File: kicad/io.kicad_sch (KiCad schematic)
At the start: 12 parts, among them J10 IO6, J5 IO1, J6 IO2, J7 IO3, J8 IO4, J9 IO5

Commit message: Lay out rev 2 with an internal pack, protector and cost-down parts
Board is 91 x 47 mm for a 96 x 52 mm enclosure, with placement and hand
power routing done; signal routing is still to do.

- Internal Gens Ace 3S 1000 mAh pack on an XT60 pigtail, protected on the
  board by a BQ7791501 with back-to-back low-side FETs and a 2.5 mOhm
  shunt, plus a balance header and two NTCs.
- USB-A and USB-C on the top edge, IO as a recessed 3 x 6 pin block, GPIO
  map re-swapped for the placement, USB nets renamed with P/N suffixes
  for the diff-pair router.
- Cost-down swaps that keep every feature: basic or preferred passives
  and ICs, cheaper connectors, a THT power switch rated for 12.6 V, and
  replacements for the low-stock TH1 and Q2/Q3. L3 is Digi-Key sourced
  and hand-placed.
- Net classes and design rules, rev 2 power-net widths in review.py, and
  the PCB critic and loop updated for rev 2.

Schematic review passes; PCB review passes every gate except unrouted.

Co-Authored-By: Claude Opus 5.5 <noreply@anthropic.com>
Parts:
- J10, J5, J6, J7, J8, J9: footprint Connector_PinHeader_2.54mm:PinHeader_1x03_P2.54mm_Horizontal -> Connector_PinHeader_2.54mm:PinHeader_1x03_P2.54mm_Vertical; LCSC Part # C32713262 -> C49257; MPN HX PZ2.54-1x3P WZ -> 2.54-1*3P; Manufacturer hanxia -> BOOMELE(Boom Precision Elec)
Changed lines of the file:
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@@
 			)
 		)
-		(property "Footprint" "Connector_PinHeader_2.54mm:PinHeader_1x03_P2.54mm_Horizontal"
+		(property "Footprint" "Connector_PinHeader_2.54mm:PinHeader_1x03_P2.54mm_Vertical"
 			(at 129.54 48.26 0)
 			(hide yes)
@@
 			)
 		)
-    (property "MPN" "HX PZ2.54-1x3P WZ" (at 129.54 48.26 0)
-      (effects (font (size 1.27 1.27)) (hide yes))
-    )
-    (property "Manufacturer" "hanxia" (at 129.54 48.26 0)
-      (effects (font (size 1.27 1.27)) (hide yes))
-    )
-    (property "LCSC Part #" "C32713262" (at 129.54 48.26 0)
+    (property "MPN" "2.54-1*3P" (at 129.54 48.26 0)
+      (effects (font (size 1.27 1.27)) (hide yes))
+    )
+    (property "Manufacturer" "BOOMELE(Boom Precision Elec)" (at 129.54 48.26 0)
+      (effects (font (size 1.27 1.27)) (hide yes))
+    )
+    (property "LCSC Part #" "C49257" (at 129.54 48.26 0)
       (effects (font (size 1.27 1.27)) (hide yes))
     )
@@
 			)
 		)
-		(property "Footprint" "Connector_PinHeader_2.54mm:PinHeader_1x03_P2.54mm_Horizontal"
+		(property "Footprint" "Connector_PinHeader_2.54mm:PinHeader_1x03_P2.54mm_Vertical"
 			(at 129.54 66.04 0)
 			(hide yes)
@@
 			)
 		)
-    (property "MPN" "HX PZ2.54-1x3P WZ" (at 129.54 66.04 0)
-      (effects (font (size 1.27 1.27)) (hide yes))
-    )
-    (property "Manufacturer" "hanxia" (at 129.54 66.04 0)
-      (effects (font (size 1.27 1.27)) (hide yes))
-    )
-    (property "LCSC Part #" "C32713262" (at 129.54 66.04 0)
+    (property "MPN" "2.54-1*3P" (at 129.54 66.04 0)
+      (effects (font (size 1.27 1.27)) (hide yes))
+    )
+    (property "Manufacturer" "BOOMELE(Boom Precision Elec)" (at 129.54 66.04 0)
+      (effects (font (size 1.27 1.27)) (hide yes))
+    )
+    (property "LCSC Part #" "C49257" (at 129.54 66.04 0)
       (effects (font (size 1.27 1.27)) (hide yes))
     )
@@
 			)
 		)
-		(property "Footprint" "Connector_PinHeader_2.54mm:PinHeader_1x03_P2.54mm_Horizontal"
+		(property "Footprint" "Connector_PinHeader_2.54mm:PinHeader_1x03_P2.54mm_Vertical"
 			(at 129.54 83.82 0)
 			(hide yes)
@@
 			)
 		)
-    (property "MPN" "HX PZ2.54-1x3P WZ" (at 129.54 83.82 0)
-      (effects (font (size 1.27 1.27)) (hide yes))
-    )
-    (property "Manufacturer" "hanxia" (at 129.54 83.82 0)
-      (effects (font (size 1.27 1.27)) (hide yes))
-    )
-    (property "LCSC Part #" "C32713262" (at 129.54 83.82 0)
+    (property "MPN" "2.54-1*3P" (at 129.54 83.82 0)
+      (effects (font (size 1.27 1.27)) (hide yes))
+    )
+    (property "Manufacturer" "BOOMELE(Boom Precision Elec)" (at 129.54 83.82 0)
+      (effects (font (size 1.27 1.27)) (hide yes))
+    )
+    (property "LCSC Part #" "C49257" (at 129.54 83.82 0)
       (effects (font (size 1.27 1.27)) (hide yes))
     )
@@
 			)
 		)
-		(property "Footprint" "Connector_PinHeader_2.54mm:PinHeader_1x03_P2.54mm_Horizontal"
+		(property "Footprint" "Connector_PinHeader_2.54mm:PinHeader_1x03_P2.54mm_Vertical"
 			(at 129.54 101.6 0)
 			(hide yes)
@@
 			)
 		)
-    (property "MPN" "HX PZ2.54-1x3P WZ" (at 129.54 101.6 0)
-      (effects (font (size 1.27 1.27)) (hide yes))
-    )
-    (property "Manufacturer" "hanxia" (at 129.54 101.6 0)
-      (effects (font (size 1.27 1.27)) (hide yes))
-    )
-    (property "LCSC Part #" "C32713262" (at 129.54 101.6 0)
+    (property "MPN" "2.54-1*3P" (at 129.54 101.6 0)
+      (effects (font (size 1.27 1.27)) (hide yes))
+    )
+    (property "Manufacturer" "BOOMELE(Boom Precision Elec)" (at 129.54 101.6 0)
+      (effects (font (size 1.27 1.27)) (hide yes))
+    )
+    (property "LCSC Part #" "C49257" (at 129.54 101.6 0)
       (effects (font (size 1.27 1.27)) (hide yes))
     )
@@
 			)
 		)
-		(property "Footprint" "Connector_PinHeader_2.54mm:PinHeader_1x03_P2.54mm_Horizontal"
+		(property "Footprint" "Connector_PinHeader_2.54mm:PinHeader_1x03_P2.54mm_Vertical"
 			(at 129.54 119.38 0)
 			(hide yes)
@@
 			)
 		)
-    (property "MPN" "HX PZ2.54-1x3P WZ" (at 129.54 119.38 0)
-      (effects (font (size 1.27 1.27)) (hide yes))
-    )
-    (property "Manufacturer" "hanxia" (at 129.54 119.38 0)
-      (effects (font (size 1.27 1.27)) (hide yes))
-    )
-    (property "LCSC Part #" "C32713262" (at 129.54 119.38 0)
+    (property "MPN" "2.54-1*3P" (at 129.54 119.38 0)
+      (effects (font (size 1.27 1.27)) (hide yes))
+    )
+    (property "Manufacturer" "BOOMELE(Boom Precision Elec)" (at 129.54 119.38 0)
+      (effects (font (size 1.27 1.27)) (hide yes))
+    )
+    (property "LCSC Part #" "C49257" (at 129.54 119.38 0)
       (effects (font (size 1.27 1.27)) (hide yes))
     )
@@
 			)
 		)
-		(property "Footprint" "Connector_PinHeader_2.54mm:PinHeader_1x03_P2.54mm_Horizontal"
+		(property "Footprint" "Connector_PinHeader_2.54mm:PinHeader_1x03_P2.54mm_Vertical"
 			(at 129.54 137.16 0)
 			(hide yes)
@@
 			)
 		)
-    (property "MPN" "HX PZ2.54-1x3P WZ" (at 129.54 137.16 0)
-      (effects (font (size 1.27 1.27)) (hide yes))
-    )
-    (property "Manufacturer" "hanxia" (at 129.54 137.16 0)
-      (effects (font (size 1.27 1.27)) (hide yes))
-    )
-    (property "LCSC Part #" "C32713262" (at 129.54 137.16 0)
-      (effects (font (size 1.27 1.27)) (hide yes))
-    )
+    (property "MPN" "2.54-1*3P" (at 129.54 137.16 0)
+      (effects (font (size 1.27 1.27)) (hide yes))
+    )
+    (property "Manufacturer" "BOOMELE(Boom Precision Elec)" (at 129.54 137.16 0)
+      (effects (font (size 1.27 1.27)) (hide yes))
+    )
+    (property "LCSC Part #" "C49257" (at 129.54 137.16 0)
+      (effects (font (size 1.27 1.27)) (hide yes))
+    )

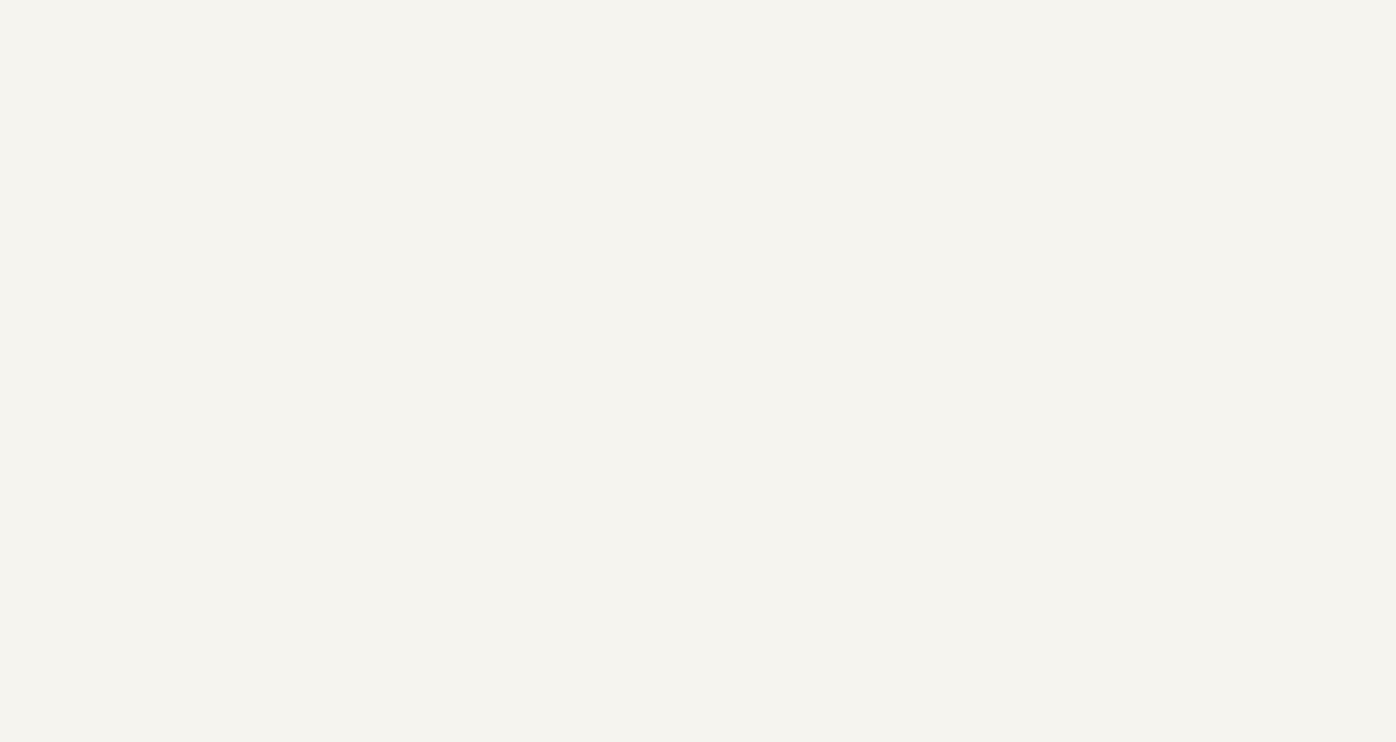
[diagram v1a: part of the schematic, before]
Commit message: Add a header for an external WS2812B LED stick
J12 (JST-PH 3-pin) feeds an 8-LED WS2812B stick mounted on the case's
top edge near the USB ports. GPIO21 drives it through a 74AHCT1G125 so
the data line reaches the 5 V VIH, with a 330 ohm series resistor and
10 uF at the connector. Power comes from the switched 5 V rail; firmware
should cap brightness (about 0.5 A at full white).

Co-Authored-By: Claude Opus 5.5 <noreply@anthropic.com>
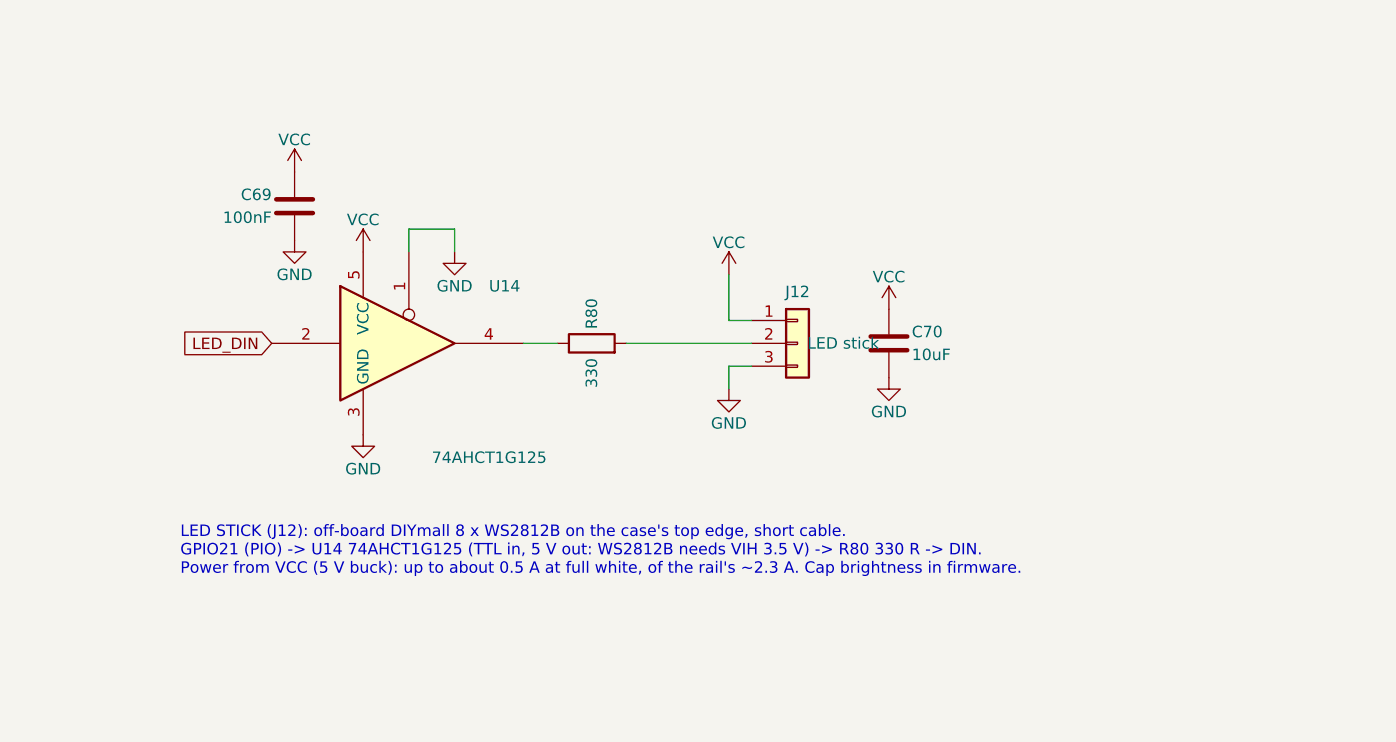
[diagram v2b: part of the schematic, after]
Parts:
- added C69: 100nF, Capacitor_SMD:C_0402_1005Metric, symbol Device:C
- added C70: 10uF, Capacitor_SMD:C_0805_2012Metric, symbol Device:C
- added J12: LED stick, Connector_JST:JST_PH_B3B-PH-K_1x03_P2.00mm_Vertical, symbol Connector_Generic:Conn_01x03
- added R80: 330, Resistor_SMD:R_0402_1005Metric, symbol Device:R
- added U14: 74AHCT1G125, Package_TO_SOT_SMD:SOT-23-5, symbol 74xGxx:74AHCT1G125
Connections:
- net GND: now also C69.2, C70.2, J12.3 (Pin_3), U14.1, U14.3 (GND)
- net VCC: now also C69.1, C70.1, J12.1 (Pin_1), U14.5 (VCC)
- new net: R80.1, U14.4
- new net: J12.2 (Pin_2), R80.2
- new net LED_DIN: U14.2
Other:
- note added: "LED STICK (J12): off-board DIYmall 8 x WS2812B on the case's top edge, short cable. GPIO21 (PIO) -> U14 74AHCT1G125 (TTL in, 5 V out: WS2812B needs VIH 3.5 V) -> R80 330 R -> DIN. Power from VCC (5 V buck): up to about 0.5 A at full white, of the rail's ~2.3 A. Cap brightness in firmware."
